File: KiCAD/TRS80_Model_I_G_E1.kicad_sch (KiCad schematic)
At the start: 3 parts

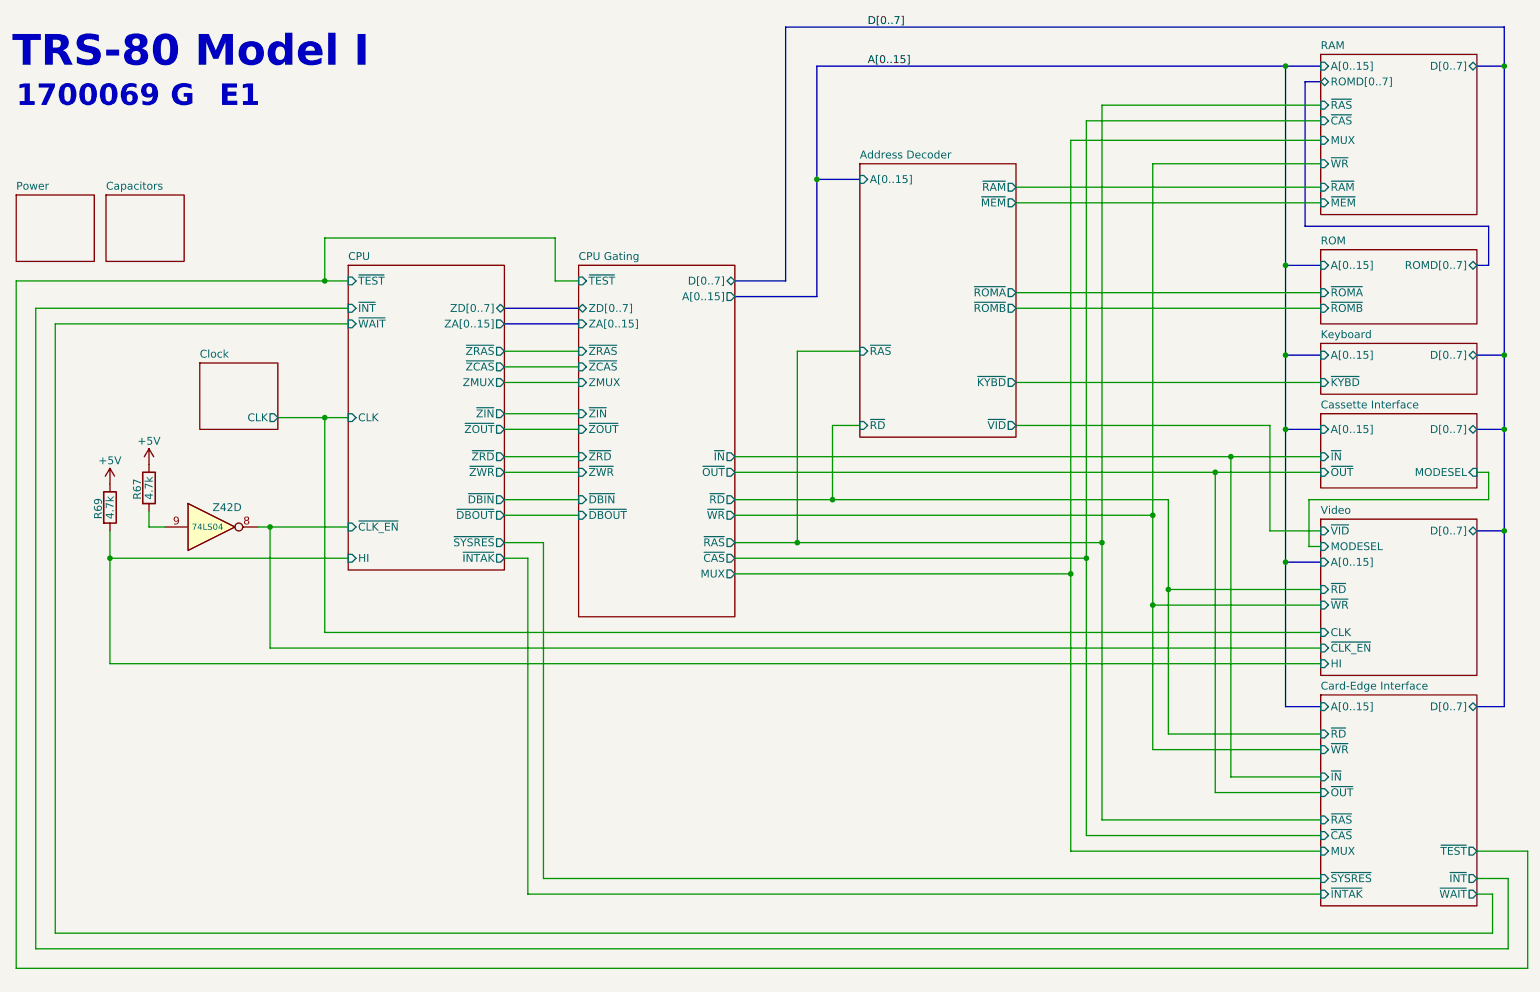
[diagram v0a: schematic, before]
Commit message: Update schematics (correct page flow) and add alternative to Q4 in BOM
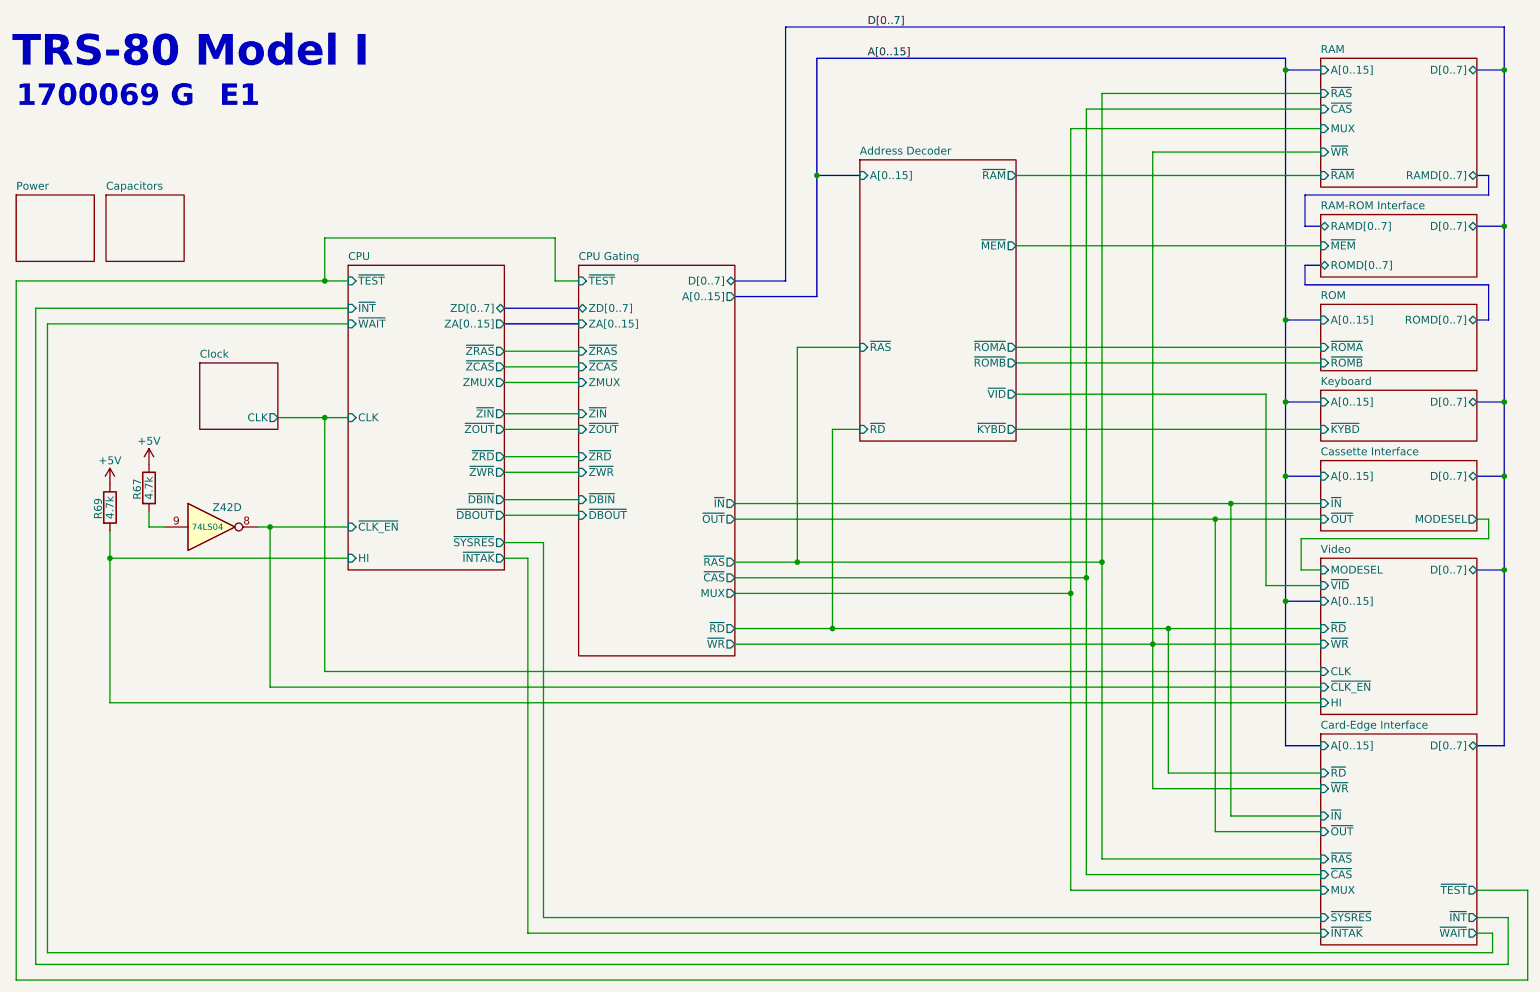
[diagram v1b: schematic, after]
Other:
- added sheet RAM-ROM Interface (RAM_ROM_Interface.kicad_sch)
- sheet RAM ports: added RAMD[0..7]; removed ROMD[0..7], ~{MEM}

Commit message: Updated revision to Rev C
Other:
- title: TRS-80 Model I G -> TRS-80 Model I Rev G
